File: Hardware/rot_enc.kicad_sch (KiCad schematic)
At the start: 0 parts

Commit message: added rotary encoder
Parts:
- added SW?: RotaryEncoder_Switch, symbol Device:RotaryEncoder_Switch
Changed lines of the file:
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@@
 (kicad_sch (version 20211123) (generator eeschema)
   (paper "A4")
+  (symbol (lib_id "Device:RotaryEncoder_Switch") (at 156.21 99.06 0) (unit 1)
+    (in_bom yes) (on_board yes) (fields_autoplaced)
+    (property "Reference" "SW?" (id 0) (at 156.21 88.9 0))
+    (property "Value" "RotaryEncoder_Switch" (id 1) (at 156.21 91.44 0))
+    (property "Footprint" "" (id 2) (at 152.4 94.996 0)
+      (effects (font (size 1.27 1.27)) hide)
+    )
+    (property "Datasheet" "~" (id 3) (at 156.21 92.456 0)
+      (effects (font (size 1.27 1.27)) hide)
+    )
+    (pin "A")
+    (pin "B")
+    (pin "C")
+    (pin "S1")
+    (pin "S2")
+  )
 )

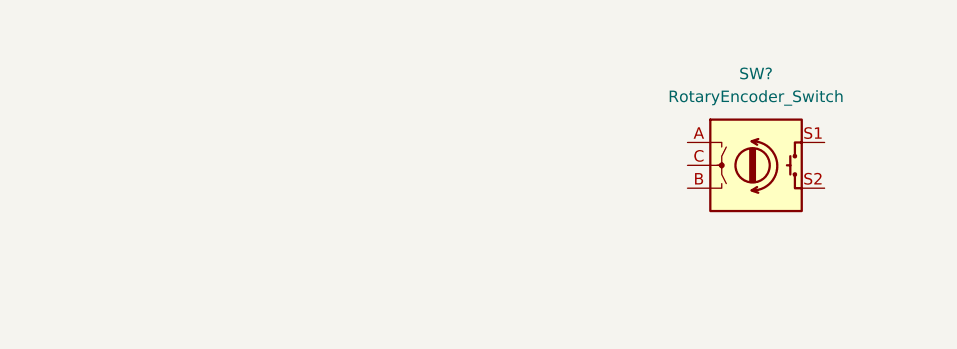
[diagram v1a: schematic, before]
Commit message: added rotary encoder parts
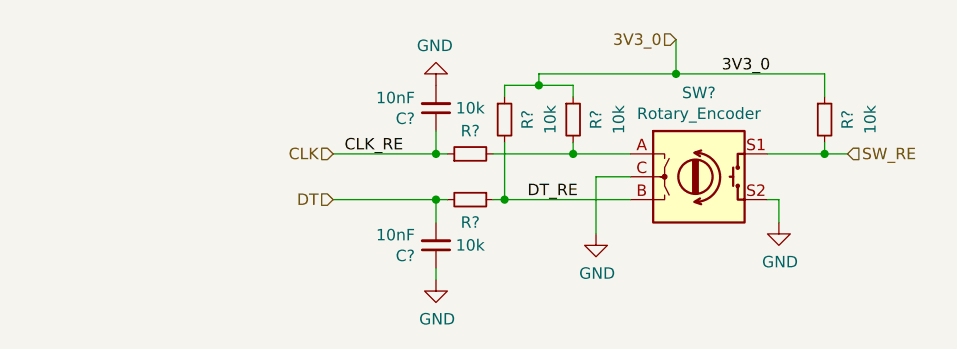
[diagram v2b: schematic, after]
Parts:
- removed SW?: RotaryEncoder_Switch, symbol Device:RotaryEncoder_Switch
- added C? (x2): 10nF, Capacitor_SMD:C_0805_2012Metric_Pad1.15x1.40mm_HandSolder, symbol Device:C_Small
- added R? (x5): 10k, Resistor_SMD:R_0805_2012Metric_Pad1.20x1.40mm_HandSolder, symbol Device:R_Small
- added SW?: Rotary_Encoder, Rotary_Encoder:RotaryEncoder_Alps_EC12E-Switch_Vertical_H20mm, symbol Device:Rotary_Encoder_Switch
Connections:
- new net: R?.2, R?.2, SW?.A
- new net 3V3_0: R?.1, R?.1, R?.1
- new net CLK: C?.1, R?.1
- new net DT: C?.2, R?.2
- new net DT_RE: R?.1, R?.2, SW?.B
- new net GND: C?.1, C?.2, SW?.C, SW?.S2
- new net SW_RE: R?.2, SW?.S1

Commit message: included psu on pcb
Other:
- company: (none) -> ncAudio
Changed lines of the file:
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@@
 (kicad_sch (version 20211123) (generator eeschema)
   (paper "A4")
+  (title_block
+    (date "2022-12-27")
+    (rev "0.1")
+    (company "ncAudio")
+  )
   (junction (at 120.65 97.79) (diameter 0) (color 0 0 0 0)
   )

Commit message: cleaned up busses
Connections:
- net 3V3_0 renamed 3V3
- net CLK renamed RotEnc.CLK
- net DT renamed RotEnc.DT
- net DT_RE: no longer names the net of R?.1, R?.2, SW?.B
- net SW_RE renamed RotEnc.SW
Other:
- moved on the sheet: R?
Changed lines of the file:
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@@
     (company "ncAudio")
   )
+  (junction (at 120.65 102.87) (diameter 0) (color 0 0 0 0)
+  )
   (junction (at 120.65 97.79) (diameter 0) (color 0 0 0 0)
   )
-  (junction (at 120.65 102.87) (diameter 0) (color 0 0 0 0)
-  )
   (junction (at 128.27 102.87) (diameter 0) (color 0 0 0 0)
   )
+  (junction (at 147.32 88.9) (diameter 0) (color 0 0 0 0)
+  )
+  (junction (at 135.89 97.79) (diameter 0) (color 0 0 0 0)
+  )
   (junction (at 163.83 97.79) (diameter 0) (color 0 0 0 0)
   )
-  (junction (at 147.32 88.9) (diameter 0) (color 0 0 0 0)
-  )
-  (junction (at 135.89 97.79) (diameter 0) (color 0 0 0 0)
-  )
   (junction (at 132.08 90.17) (diameter 0) (color 0 0 0 0)
   )
+  (bus_entry (at 97.79 95.25) (size 2.54 2.54)
+    (stroke (width 0) (type default) (color 0 0 0 0))
+  )
+  (bus_entry (at 97.79 90.17) (size 2.54 2.54)
+    (stroke (width 0) (type default) (color 0 0 0 0))
+  )
+  (bus_entry (at 97.79 100.33) (size 2.54 2.54)
+    (stroke (width 0) (type default) (color 0 0 0 0))
+  )
   (wire (pts (xy 142.24 97.79) (xy 135.89 97.79))
     (stroke (width 0) (type default) (color 0 0 0 0))
@@
     (stroke (width 0) (type default) (color 0 0 0 0))
   )
-  (wire (pts (xy 109.22 102.87) (xy 120.65 102.87))
+  (wire (pts (xy 100.33 92.71) (xy 111.76 92.71))
     (stroke (width 0) (type default) (color 0 0 0 0))
   )
@@
     (stroke (width 0) (type default) (color 0 0 0 0))
   )
+  (bus (pts (xy 97.79 95.25) (xy 97.79 100.33))
+    (stroke (width 0) (type default) (color 0 0 0 0))
+  )
   (wire (pts (xy 147.32 88.9) (xy 163.83 88.9))
     (stroke (width 0) (type default) (color 0 0 0 0))
@@
     (stroke (width 0) (type default) (color 0 0 0 0))
   )
+  (bus (pts (xy 97.79 85.09) (xy 97.79 90.17))
+    (stroke (width 0) (type default) (color 0 0 0 0))
+  )
+  (wire (pts (xy 163.83 97.79) (xy 176.53 97.79))
+    (stroke (width 0) (type default) (color 0 0 0 0))
+  )
   (wire (pts (xy 127 97.79) (xy 135.89 97.79))
     (stroke (width 0) (type default) (color 0 0 0 0))
@@
     (stroke (width 0) (type default) (color 0 0 0 0))
   )
-  (wire (pts (xy 163.83 97.79) (xy 166.37 97.79))
-    (stroke (width 0) (type default) (color 0 0 0 0))
-  )
   (wire (pts (xy 128.27 96.52) (xy 128.27 102.87))
     (stroke (width 0) (type default) (color 0 0 0 0))
@@
     (stroke (width 0) (type default) (color 0 0 0 0))
   )
+  (wire (pts (xy 100.33 97.79) (xy 120.65 97.79))
+    (stroke (width 0) (type default) (color 0 0 0 0))
+  )
   (wire (pts (xy 120.65 95.25) (xy 120.65 97.79))
     (stroke (width 0) (type default) (color 0 0 0 0))
@@
     (stroke (width 0) (type default) (color 0 0 0 0))
   )
+  (wire (pts (xy 120.65 88.9) (xy 120.65 90.17))
+    (stroke (width 0) (type default) (color 0 0 0 0))
+  )
+  (wire (pts (xy 100.33 102.87) (xy 120.65 102.87))
+    (stroke (width 0) (type default) (color 0 0 0 0))
+  )
   (wire (pts (xy 135.89 90.17) (xy 135.89 91.44))
     (stroke (width 0) (type default) (color 0 0 0 0))
@@
     (stroke (width 0) (type default) (color 0 0 0 0))
   )
-  (wire (pts (xy 163.83 96.52) (xy 163.83 97.79))
-    (stroke (width 0) (type default) (color 0 0 0 0))
-  )
-  (wire (pts (xy 109.22 97.79) (xy 120.65 97.79))
+  (wire (pts (xy 163.83 95.25) (xy 163.83 97.79))
+    (stroke (width 0) (type default) (color 0 0 0 0))
+  )
+  (bus (pts (xy 97.79 90.17) (xy 97.79 95.25))
+    (stroke (width 0) (type default) (color 0 0 0 0))
+  )
+  (wire (pts (xy 140.97 85.09) (xy 147.32 85.09))
     (stroke (width 0) (type default) (color 0 0 0 0))
   )
@@
     (stroke (width 0) (type default) (color 0 0 0 0))
   )
-  (wire (pts (xy 163.83 88.9) (xy 163.83 91.44))
+  (wire (pts (xy 163.83 88.9) (xy 163.83 90.17))
     (stroke (width 0) (type default) (color 0 0 0 0))
   )
@@
     (stroke (width 0) (type default) (color 0 0 0 0))
   )
-  (label "DT_RE" (at 130.81 102.87 0)
+  (label "RotEnc.DT" (at 101.6 102.87 0)
     (effects (font (size 1.27 1.27)) (justify left bottom))
   )
-  (label "3V3_0" (at 152.3956 88.9 0)
+  (label "RotEnc.SW" (at 111.76 92.71 180)
+    (effects (font (size 1.27 1.27)) (justify right bottom))
+  )
+  (label "RotEnc.SW" (at 176.53 97.79 180)
+    (effects (font (size 1.27 1.27)) (justify right bottom))
+  )
+  (label "RotEnc.CLK" (at 101.6 97.79 0)
     (effects (font (size 1.27 1.27)) (justify left bottom))
   )
-  (label "CLK_RE" (at 110.49 97.79 0)
+  (label "3V3" (at 142.24 85.09 0)
     (effects (font (size 1.27 1.27)) (justify left bottom))
   )
-  (hierarchical_label "SW_RE" (shape input) (at 166.37 97.79 0)
-    (effects (font (size 1.27 1.27)) (justify left))
-  )
-  (hierarchical_label "3V3_0" (shape input) (at 147.32 85.09 180)
+  (hierarchical_label "3V3" (shape input) (at 140.97 85.09 180)
     (effects (font (size 1.27 1.27)) (justify right))
   )
-  (hierarchical_label "CLK" (shape input) (at 109.22 97.79 180)
-    (effects (font (size 1.27 1.27)) (justify right))
-  )
-  (hierarchical_label "DT" (shape input) (at 109.22 102.87 180)
+  (hierarchical_label "RotEnc{SW DT CLK}" (shape input) (at 97.79 85.09 180)
     (effects (font (size 1.27 1.27)) (justify right))
   )
@@
     (pin "S2")
   )
-  (symbol (lib_id "power:GND") (at 120.65 90.17 180) (unit 1)
-    (in_bom yes) (on_board yes)
-    (property "Reference" "#PWR?" (id 0) (at 120.65 83.82 0)
-      (effects (font (size 1.27 1.27)) hide)
-    )
-    (property "Value" "GND" (id 1) (at 120.523 85.7758 0))
-    (property "Footprint" "" (id 2) (at 120.65 90.17 0)
-      (effects (font (size 1.27 1.27)) hide)
-    )
-    (property "Datasheet" "" (id 3) (at 120.65 90.17 0)
+  (symbol (lib_id "power:GND") (at 120.65 88.9 180) (unit 1)
+    (in_bom yes) (on_board yes)
+    (property "Reference" "#PWR?" (id 0) (at 120.65 82.55 0)
+      (effects (font (size 1.27 1.27)) hide)
+    )
+    (property "Value" "GND" (id 1) (at 120.523 84.5058 0))
+    (property "Footprint" "" (id 2) (at 120.65 88.9 0)
+      (effects (font (size 1.27 1.27)) hide)
+    )
+    (property "Datasheet" "" (id 3) (at 120.65 88.9 0)
       (effects (font (size 1.27 1.27)) hide)
     )
@@
     (pin "2")
   )
-  (symbol (lib_id "Device:R_Small") (at 163.83 93.98 0) (unit 1)
-    (in_bom yes) (on_board yes)
-    (property "Reference" "R?" (id 0) (at 166.37 93.98 90))
-    (property "Value" "10k" (id 1) (at 168.91 93.98 90))
-    (property "Footprint" "Resistor_SMD:R_0805_2012Metric_Pad1.20x1.40mm_HandSolder" (id 2) (at 163.83 93.98 0)
-      (effects (font (size 1.27 1.27)) hide)
-    )
-    (property "Datasheet" "~" (id 3) (at 163.83 93.98 0)
-      (effects (font (size 1.27 1.27)) hide)
-    )
+  (symbol (lib_id "Device:R_Small") (at 163.83 92.71 0) (unit 1)
+    (in_bom yes) (on_board yes)
+    (property "Reference" "R?" (id 0) (at 166.37 92.71 90))
+    (property "Value" "10k" (id 1) (at 168.91 92.71 90))
+    (property "Footprint" "Resistor_SMD:R_0805_2012Metric_Pad1.20x1.40mm_HandSolder" (id 2) (at 163.83 92.71 0)
+      (effects (font (size 1.27 1.27)) hide)
+    )
+    (property "Datasheet" "~" (id 3) (at 163.83 92.71 0)
+      (effects (font (size 1.27 1.27)) hide)
+    )
